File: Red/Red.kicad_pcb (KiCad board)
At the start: 4 copper layers, 64 x 100 mm, 83 parts, among them IC701 STM32G473CET6, J201 Conn_01x02, J301 Conn_01x03, J302 Screw_Terminal_01x02, J303 Screw_Terminal_01x02, J701 Conn_01x06, J801 USB_C_Receptacle, J802 Conn_01x10, J803 Conn_01x10, Q301 DMG3414U, Q302 DMG3414U, Q303 DMG3414U, Q304 DMG3414U, Q305 DMG3414U, SW701 SW_Push, U201 AZ1117-3.3, U202 AZ1117-5.0, U501 MPL115A1, U502 ICM-20948, U701 MAX7375AXR805, U801 FT230XS, Y701 SIT1533AI-H4-DCC-32.768E

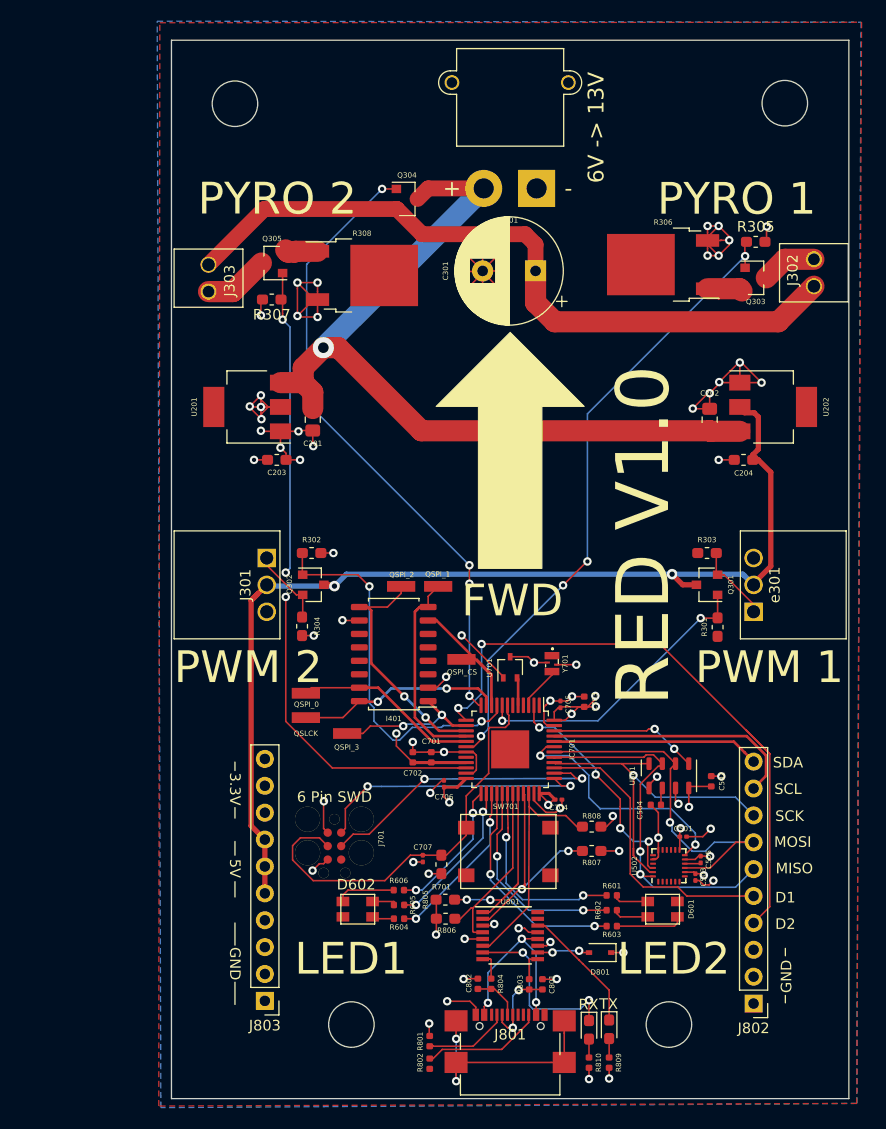
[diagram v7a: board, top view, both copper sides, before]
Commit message: Created V1.1 Layout, minor schematic updates
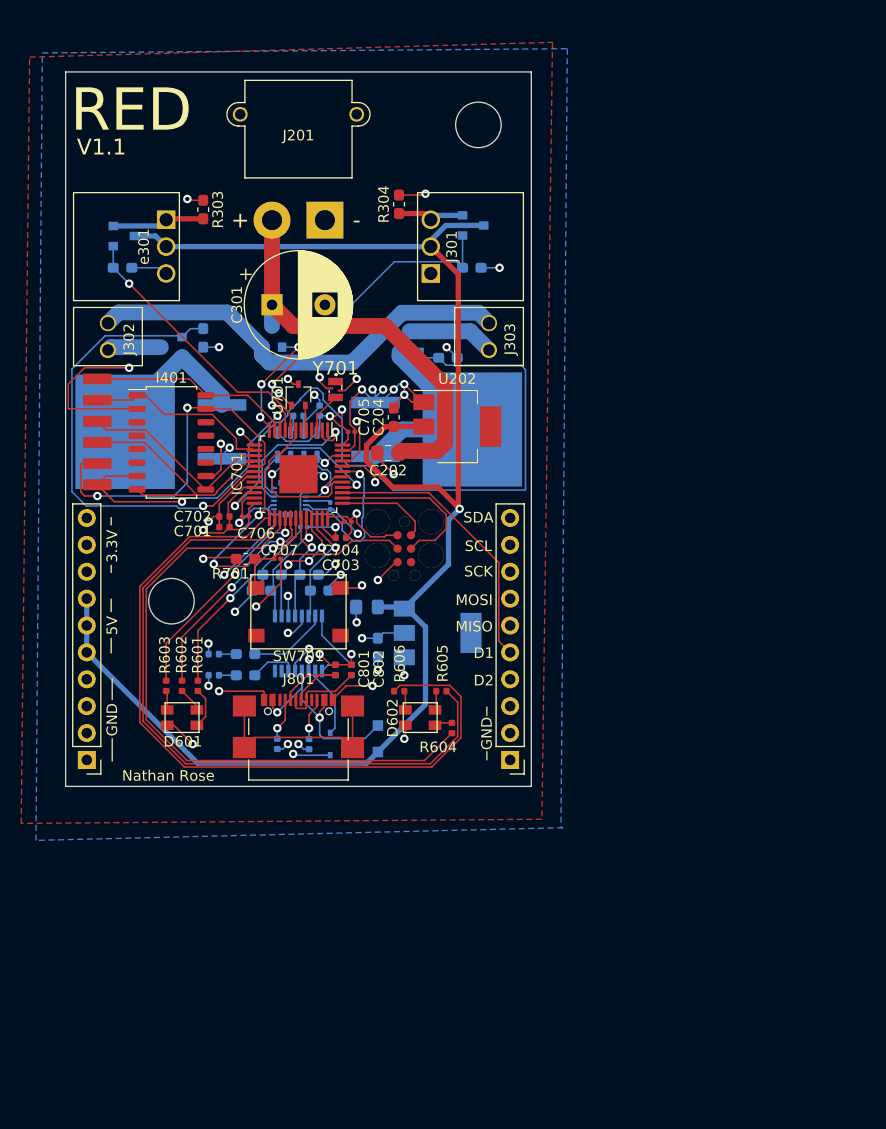
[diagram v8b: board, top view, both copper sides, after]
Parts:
- removed H103, H104: MountingHole, MountingHole:MountingHole_4.3mm_M4
- added D804: LEDG, Diode_SMD:D_0603_1608Metric_Pad1.05x0.95mm_HandSolder, B.Cu at (114.0, 111.0)
- C201, C203, C501, C502, C503, C504, C505, Q301, Q302, Q303, Q304, Q305, R301, R302, R305, R307, R801, R802, R803, R804, R805, R806, R807, R808, R809, R810, U201, U501, U502, U801: moved to B.Cu
- D801: value D -> D_Schottky; footprint Diode_SMD:D_SOD-323 -> Diode_SMD:D_SOD-323_HandSoldering; moved to B.Cu
- D802: value LEDY -> D; footprint Diode_SMD:D_0603_1608Metric_Pad1.05x0.95mm_HandSolder -> Diode_SMD:D_SOD-323; moved to B.Cu
- D803: value LEDG -> LEDY; moved to B.Cu
- R306, R308: footprint Red:dpak_back_isolated -> Package_TO_SOT_SMD:TO-263-2_TabPin1; moved to B.Cu
- Y701: footprint SIT1533AIH4DCC32768E -> Red:SIT1533AIH4DCC32768E
- moved H102 86.9 mm to (136.0, 61.0)
- moved J302 67.0 mm to (101.0, 81.0), turned to 270 degrees
- moved R301 65.7 mm to (102.4, 74.5), turned to 0 degrees
- moved Q301 64.2 mm to (102.5, 71.5), turned to 0 degrees
- moved e301 64.0 mm to (106.5, 72.5), turned to 270 degrees
- moved R303 57.6 mm to (110.0, 69.0), turned to 90 degrees
- moved Q303 55.6 mm to (107.0, 82.0), turned to 180 degrees
- moved R305 53.0 mm to (110.0, 81.1), turned to 270 degrees
- moved R810 52.4 mm to (111.0, 111.0), turned to 180 degrees
- moved R809 52.3 mm to (111.0, 113.0), turned to 0 degrees
- moved C503 52.2 mm to (120.6, 94.2), turned to 270 degrees
- moved C502 50.9 mm to (121.0, 88.0)
- moved R306 50.0 mm to (106.0, 90.0)
- moved C504 49.9 mm to (119.0, 88.5), turned to 0 degrees
- moved U502 49.9 mm to (118.2, 96.3), turned to 270 degrees
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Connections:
- C201 pad 1: +BATT -> +5V
- C301 pad 1: Net-(C301-Pad1) -> +BATT
- D801 pad 1: +3V3 -> +5V
- D801 pad 2: Net-(D801-Pad2) -> VBUS
- D802 pad 1: Net-(D802-Pad1) -> +3V3
- J301 pad 1: /Robotics/5V_PWM2 -> GND
- J301 pad 3: GND -> /Robotics/5V_PWM2
- J302 pad 1: Net-(C301-Pad1) -> Net-(J302-Pad1)
- J303 pad 1: Net-(C301-Pad1) -> Net-(J302-Pad1)
- Q304 pad 2: Net-(C301-Pad1) -> Net-(J302-Pad1)
- R809 pad 2: Net-(D802-Pad2) -> Net-(D803-Pad2)
- R810 pad 1: Net-(D803-Pad2) -> Net-(D804-Pad2)
- U201 pad 3: +BATT -> +5V
- U801 pad 10: Net-(D801-Pad2) -> Net-(D802-Pad2)
- U801 pad 14: Net-(D802-Pad1) -> Net-(D803-Pad1)
- U801 pad 7: Net-(D803-Pad1) -> Net-(D804-Pad1)
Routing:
- net Net-(C301-Pad1): track 68.4 -> 0.00 mm
- net /Microprocessor/LED2_B: track 13.2 -> 72.0 mm, vias 2 -> 0
- net /Microprocessor/LED2_G: track 14.7 -> 65.4 mm, vias 2 -> 0
- net /Microprocessor/ARM: track 60.0 -> 11.2 mm, vias 4 -> 3
- net +5V: track 101.6 -> 146.7 mm, vias 2 -> 1
- net /RGBLEDs/LED2_B: track 15.9 -> 59.9 mm, vias 2 -> 0
- net Net-(J302-Pad1): track 0.00 -> 41.2 mm
- net +BATT: track 79.7 -> 39.7 mm, vias 1 -> 0
- net GND: track 163.5 -> 135.8 mm, vias 54 -> 39
- net /Microprocessor/SWDIO: track 26.4 -> 9.05 mm, vias 2 -> 0
- net Net-(Q305-Pad2): track 3.12 -> 20.3 mm
- net /FLash/QSPI_IO0: track 17.5 -> 33.9 mm, vias 0 -> 2
- net /Robotics/FIRE1: track 60.2 -> 45.0 mm, vias 4 -> 1
- net +3V3: track 78.1 -> 92.6 mm, vias 28 -> 17
- net Net-(D803-Pad1): track 17.2 -> 4.47 mm, vias 2 -> 0
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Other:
- board size 64 x 100 mm -> 44 x 67.5 mm
- net class 3.3V removed
- rule pad_to_mask_clearance: 0.05 -> 0.025
- rule solder_mask_min_width: 0.1 -> 0.05
- board text added: "Nathan Rose"
- board text added: "RED"
- board text added: "V1.1"
- board text removed: "3 amp Channel"
- board text removed: "3.3V Regulation"
- board text removed: "5V PWM"
- board text removed: "5V Regulation"
- board text removed: "6 Pin SWD"
- board text removed: "6V -> 13V"
- board text removed: "Arm For 3 Amp channels"
- board text removed: "BAROMETER"
- board text removed: "CLOCKS"
- board text removed: "Cap for 3 Amp Channels"
- board text removed: "FLASH with QSPI"
- board text removed: "FTDI"
- board text removed: "FWD"
- board text removed: "IMU"
- board text removed: "IO Pins"
- board text removed: "LED1"
- board text removed: "LED2"
- board text removed: "PWM 1"
- board text removed: "PWM 2"
- board text removed: "PYRO 1"
- board text removed: "PYRO 2"
- board text removed: "Power Pins"
- board text removed: "QSLCK"
- board text removed: "QSPI_0"
- board text removed: "QSPI_1"
- board text removed: "QSPI_2"
- board text removed: "QSPI_3"
- board text removed: "QSPI_CS"
- board text removed: "RED V1.0"
- board text removed: "RESET BUTTON"
- board text removed: "RGB LED"
- board text removed: "RX"
- board text removed: "STM32"
- board text removed: "SWD"
- board text removed: "TX"
- board text removed: "USBC"
- board text removed: "XT30"
